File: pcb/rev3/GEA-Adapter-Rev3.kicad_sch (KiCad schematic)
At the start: 89 parts, among them J1 8P8C, J2 1x6, J3 TC2030, J4 USB_C_Receptacle_USB2.0_16P, Q1 Si2309CDS, Q2 Si2309CDS, SW1 SW_Push, SW2 SW_Push, U2 ESP32-C3-WROOM-02, U4 74LVC2G07, U5 74LVC2G07_3v3, U6 AP2112K-3.3, U7 USBLC6-2SC6, U8 AP63205WU

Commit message: feat(pcb): add rev3a automatic power and USB design
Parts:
- removed C8: 1u, Capacitor_SMD:C_0805_2012Metric, symbol Device:C
- removed D12, D13: BZX84C12LT1G, Package_TO_SOT_SMD:SOT-23, symbol Diode:BZX84Cxx
- removed D7: DNI, Diode_SMD:D_SMA, symbol Device:D_TVS
- removed JP2: AltPwr, Jumper:SolderJumper-3_P1.3mm_Bridged12_RoundedPad1.0x1.5mm_NumberLabels, symbol Jumper:SolderJumper_3_Bridged12
- removed Q1, Q2: Si2309CDS, Package_TO_SOT_SMD:SOT-23, symbol Device:Q_PMOS_GSD
- removed R30, R9: 9.1k, Resistor_SMD:R_0805_2012Metric, symbol Device:R
- removed R8: DNP, Resistor_SMD:R_0805_2012Metric, symbol Device:R
- added C18, C19: 100pF, Capacitor_SMD:C_0402_1005Metric, symbol Device:C
- added C20, C21: 1u 50V X7R, Capacitor_SMD:C_0805_2012Metric, symbol Device:C
- added C22, C23: 22nF, Capacitor_SMD:C_0402_1005Metric, symbol Device:C
- added C24, C25: 100nF, Capacitor_SMD:C_0805_2012Metric, symbol Device:C
- added D14, D15, D16, D17: MBR0540-TP, Diode_SMD:D_SOD-123, symbol Diode:MBR0540
- added Q3, Q4: CJ3407, Package_TO_SOT_SMD:SOT-23, symbol Device:Q_PMOS_GSD
- added Q5: MMBT3904, Package_TO_SOT_SMD:SOT-23, symbol Transistor_BJT:MMBT3904
- added R31, R32: 5.1k, Resistor_SMD:R_0805_2012Metric, symbol Device:R
- added R33, R34: 51R, Resistor_SMD:R_0805_2012Metric, symbol Device:R
- added R35, R36, R37: 10k, Resistor_SMD:R_0805_2012Metric, symbol Device:R
- added TP10: PIN1_PROTECTED, TestPoint:TestPoint_Pad_D1.0mm, symbol Connector:TestPoint
- added TP11: PIN3_PROTECTED, TestPoint:TestPoint_Pad_D1.0mm, symbol Connector:TestPoint
- added TP12: PIN1_SW_OUT, TestPoint:TestPoint_Pad_D1.0mm, symbol Connector:TestPoint
- added TP13: PIN3_SW_OUT, TestPoint:TestPoint_Pad_D1.0mm, symbol Connector:TestPoint
- added TP14: USB_VBUS, TestPoint:TestPoint_Pad_D1.0mm, symbol Connector:TestPoint
- added TP8: PIN1_FUSED, TestPoint:TestPoint_Pad_D1.0mm, symbol Connector:TestPoint
- added TP9: PIN3_FUSED, TestPoint:TestPoint_Pad_D1.0mm, symbol Connector:TestPoint
- added U10, U9: TPS22810DBVR, Package_TO_SOT_SMD:SOT-23-6, symbol Power_Management:TPS22810DBV
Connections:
- net p1 is gone; now on net V_INPUT: TP3.1
- net GND: now also C20.2, C21.2, C22.2, C23.2, C24.2, C25.2, D16.1 (K), D17.1 (K), Q5.2 (E), R37.2, U10.2 (GND), U9.2 (GND)
- net USB_VBUS: now also TP14.1
- net PIN1_FUSED: now reaches F2.2
- net PIN1_FUSED: now also C18.1, Q3.2 (S), R31.1, TP8.1
- net PIN3_FUSED: now reaches F1.2
- net PIN3_FUSED: now also C19.1, Q4.2 (S), R32.1, TP9.1
- net APPLIANCE_PROTECTED renamed V_INPUT
- net V_INPUT: now also D14.1 (K), D15.1 (K)
- net MCU_USB_DN renamed USB_MCU_N
- net MCU_USB_DP renamed USB_MCU_P
- net USB_DN_CONN renamed USB_CONN_N
- net USB_DN_PROTECTED renamed USB_PROTECTED_N
- net USB_DP_CONN renamed USB_CONN_P
- net USB_DP_PROTECTED renamed USB_PROTECTED_P
- new net PIN1_CT: C22.1, U9.4 (CT)
- new net PIN1_GATE: Q3.1 (G), R33.2
- new net PIN1_GATE_CLAMP: C18.2, D16.2 (A), R31.2, R33.1
- new net PIN1_PROTECTED: C20.1, Q3.3 (D), R35.1, TP10.1, U9.1 (VIN), U9.3 (EN/UVLO)
- new net PIN1_SW_OUT: C24.1, D14.2 (A), TP12.1, U9.6 (VOUT)
- new net PIN3_CT: C23.1, U10.4 (CT)
- new net PIN3_EN: Q5.3 (C), R36.2, U10.3 (EN/UVLO)
- new net PIN3_GATE: Q4.1 (G), R34.2
- new net PIN3_GATE_CLAMP: C19.2, D17.2 (A), R32.2, R34.1
- new net PIN3_PROTECTED: C21.1, Q4.3 (D), R36.1, TP11.1, U10.1 (VIN)
- new net PIN3_SW_OUT: C25.1, D15.2 (A), TP13.1, U10.6 (VOUT)
- new net PRIORITY_BASE: Q5.1 (B), R35.2, R37.1
- no-connect marks 10 -> 12
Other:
- note added: "DIAGNOSTIC TEST PADS Optional top-side SMD pads for bring-up"

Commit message: fix(pcb): align rev3a appliance connector metadata
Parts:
- J1: footprint Connector_RJ:RJ45_Amphenol_54602-x08_Horizontal -> OnionStraws:RJ45_EVERCOM_5301-8P8C_Horizontal; LCSC C2847314 -> C3097717; MPN 54602-908LF -> 5301-8P8C; Manufacturer Amphenol Communications Solutions -> EVERCOM
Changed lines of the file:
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@@
 			)
 		)
-		(property "Footprint" "Connector_RJ:RJ45_Amphenol_54602-x08_Horizontal"
+		(property "Footprint" "OnionStraws:RJ45_EVERCOM_5301-8P8C_Horizontal"
 			(at 43.815 94.615 90)
 			(effects
@@
 			)
 		)
-		(property "Datasheet" "https://cdn.amphenol-cs.com/media/wysiwyg/files/drawing/c-bmj-0102.pdf"
+		(property "Datasheet" "https://jlcpcb.com/partdetail/EVERCOM-53018P8C/C3097717"
 			(at 43.815 94.615 90)
 			(effects
@@
 			)
 		)
-		(property "Description" "Amphenol Cat 3 single modular jack, horizontal through-hole, 8P8C, unshielded"
+		(property "Description" "EVERCOM horizontal through-hole 8P8C appliance connector"
 			(at 43.815 95.25 0)
 			(effects
@@
 			)
 		)
-		(property "LCSC" "C2847314"
+		(property "LCSC" "C3097717"
 			(at 43.815 95.25 0)
 			(effects
@@
 			)
 		)
-		(property "Manufacturer" "Amphenol Communications Solutions"
+		(property "Manufacturer" "EVERCOM"
 			(at 43.815 95.25 0)
 			(effects
@@
 			)
 		)
-		(property "MPN" "54602-908LF"
+		(property "MPN" "5301-8P8C"
 			(at 43.815 95.25 0)
 			(effects

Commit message: fix(pcb): correct rev3a capacitor sourcing
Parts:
- C10: LCSC C28233 -> C286510; MPN GCM188L81H104KA57 -> 0603B104M500NT; Manufacturer Murata -> FH
- C9: LCSC C15850 -> C303950; MPN CGA5L1X7R1H106K160AC -> 1206B106K500NT; Manufacturer TDK -> FH
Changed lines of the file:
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@@
 			)
 		)
-		(property "Datasheet" "~"
+		(property "Datasheet" "https://jlcpcb.com/partdetail/288017-1206B106K500NT/C303950"
 			(at 247.65 54.61 0)
 			(effects
@@
 			)
 		)
-		(property "Description" "C15850"
+		(property "Description" "10 uF 50 V X7R 1206 MLCC"
 			(at 247.65 54.61 0)
 			(effects
@@
 			)
 		)
-		(property "LCSC" "C15850"
+		(property "LCSC" "C303950"
 			(at 247.65 54.61 0)
 			(effects
@@
 			)
 		)
-		(property "Manufacturer" "TDK"
+		(property "Manufacturer" "FH"
 			(at 247.65 54.61 0)
 			(effects
@@
 			)
 		)
-		(property "MPN" "CGA5L1X7R1H106K160AC"
+		(property "MPN" "1206B106K500NT"
 			(at 247.65 54.61 0)
 			(effects
@@
 			)
 		)
-		(property "Datasheet" "~"
+		(property "Datasheet" "https://jlcpcb.com/partdetail/0603B104M500NT/C286510"
 			(at 260.35 54.61 0)
 			(effects
@@
 			)
 		)
-		(property "Description" "C28233"
+		(property "Description" "100 nF 50 V X7R 0603 MLCC"
 			(at 260.35 54.61 0)
 			(effects
@@
 			)
 		)
-		(property "LCSC" "C28233"
+		(property "LCSC" "C286510"
 			(at 260.35 54.61 0)
 			(effects
@@
 			)
 		)
-		(property "Manufacturer" "Murata"
+		(property "Manufacturer" "FH"
 			(at 260.35 54.61 0)
 			(effects
@@
 			)
 		)
-		(property "MPN" "GCM188L81H104KA57"
+		(property "MPN" "0603B104M500NT"
 			(at 260.35 54.61 0)
 			(effects

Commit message: feat(pcb): route grounds and refine rev3a sourcing
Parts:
- J4: LCSC (none) -> C2894897; MPN USB4105-GF-A -> HC-TYPE-C-16P-01A; Manufacturer GCT -> HCTL
- L1: LCSC (none) -> C412309
- U8: LCSC (none) -> C2071056
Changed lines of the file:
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@@
 			)
 		)
-		(property "Datasheet" "https://www.usb.org/sites/default/files/documents/usb_type-c.zip"
+		(property "Datasheet" "https://datasheet.lcsc.com/datasheet/pdf/7d87e82d7c94fc2f1ad4584993e52b86.pdf?productCode=C2894897"
 			(at 93.81 335.0 0)
 			(hide yes)
@@
 			)
 		)
-		(property "Description" "USB 2.0-only 16P Type-C Receptacle connector"
+		(property "Description" "HCTL USB 2.0 Type-C receptacle, 16 contacts, top mount"
 			(at 90.0 335.0 0)
 			(hide yes)
@@
 			)
 		)
-		(property "Manufacturer" "GCT"
+		(property "Manufacturer" "HCTL"
 			(at 90.0 335.0 0)
 			(effects
@@
 			)
 		)
-		(property "MPN" "USB4105-GF-A"
+		(property "MPN" "HC-TYPE-C-16P-01A"
+			(at 90.0 335.0 0)
+			(effects
+				(font
+					(size 1.27 1.27)
+				)
+				(hide yes)
+			)
+		)
+		(property "LCSC" "C2894897"
 			(at 90.0 335.0 0)
 			(effects
@@
 			)
 		)
+		(property "LCSC" "C2071056"
+			(at 250.19 80.01 0)
+			(effects
+				(font
+					(size 1.27 1.27)
+				)
+				(hide yes)
+			)
+		)
 		(property "Input_Range" "3.8V to 32V"
 			(at 250.19 80.01 0)
@@
 			(at 284.48 77.47 0)
 			(effects
+				(font
+					(size 1.27 1.27)
+				)
+				(hide yes)
+			)
+		)
+		(property "LCSC" "C412309"
+			(at 284.48 77.47 0)
+			(effects

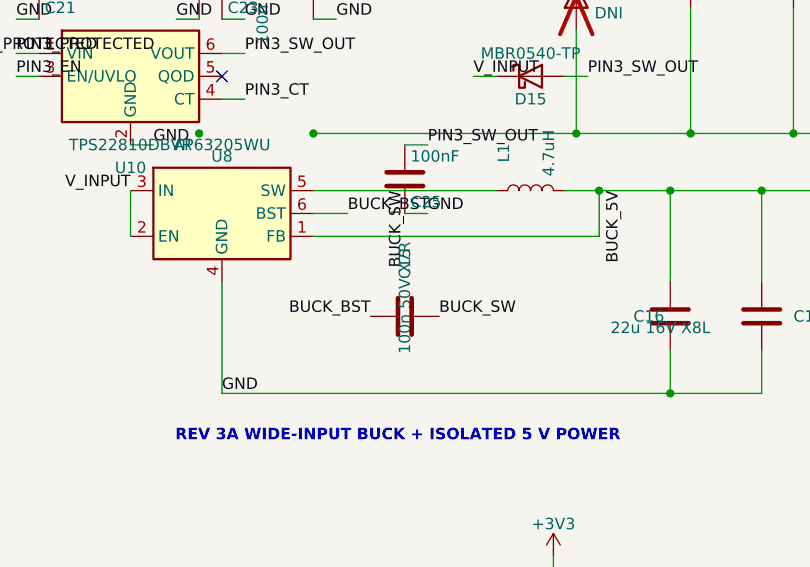
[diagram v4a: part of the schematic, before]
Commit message: fix(pcb): complete rev3a sourcing metadata
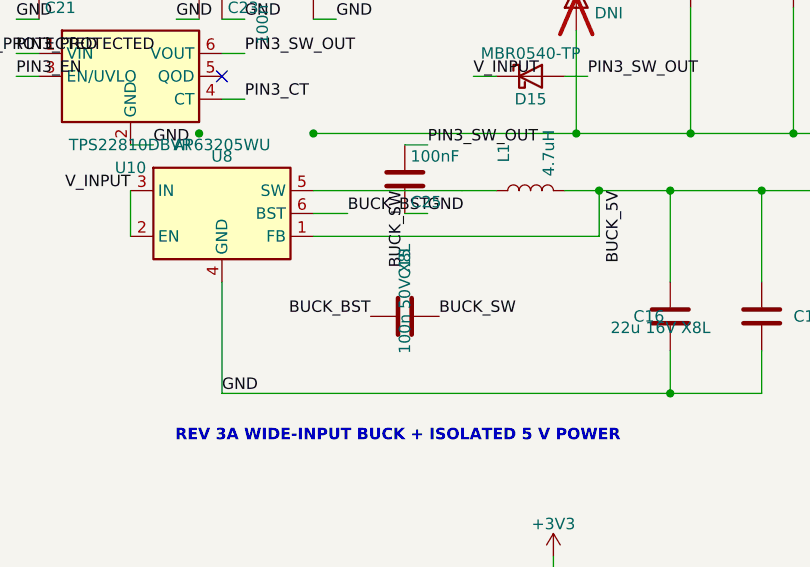
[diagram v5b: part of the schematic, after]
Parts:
- C15: value 100n 50V X7R -> 100n 50V X8L; Dielectric X7R -> X8L; LCSC (none) -> C161181
- D10, D11: LCSC (none) -> C82288
- F3: LCSC (none) -> C163512
- R26, R27: LCSC (none) -> C105580
- R28, R29: LCSC (none) -> C107701
- U7: LCSC (none) -> C7519
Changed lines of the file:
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@@
 			)
 		)
+    (property "LCSC" "C105580" (at 135.0 360.0 0)
+      (effects (font (size 1.27 1.27)) (hide yes))
+    )
 		(pin "1"
 		)
@@
 			)
 		)
+    (property "LCSC" "C105580" (at 135.0 380.0 0)
+      (effects (font (size 1.27 1.27)) (hide yes))
+    )
 		(pin "1"
 		)
@@
 			)
 		)
+    (property "LCSC" "C107701" (at 245.0 325.0 0)
+      (effects (font (size 1.27 1.27)) (hide yes))
+    )
 		(pin "1"
 		)
@@
 			)
 		)
+    (property "LCSC" "C107701" (at 245.0 345.0 0)
+      (effects (font (size 1.27 1.27)) (hide yes))
+    )
 		(pin "1"
 		)
@@
 			)
 		)
+    (property "LCSC" "C163512" (at 165.0 400.0 0)
+      (effects (font (size 1.27 1.27)) (hide yes))
+    )
 		(pin "1"
 		)
@@
 			)
 		)
+    (property "LCSC" "C7519" (at 180.0 335.0 0)
+      (effects (font (size 1.27 1.27)) (hide yes))
+    )
 		(pin "1"
 		)
@@
 			)
 		)
+    (property "LCSC" "C82288" (at 230.0 400.0 0)
+      (effects (font (size 1.27 1.27)) (hide yes))
+    )
 		(pin "1"
 		)
@@
 			)
 		)
-		(property "Value" "100n 50V X7R"
+		(property "Value" "100n 50V X8L"
 			(at 270.51 95.6 0)
 			(show_name no)
@@
 			)
 		)
-		(property "Description" "Unpolarized capacitor"
+		(property "Description" "100 nF 50 V X8L 0603 MLCC"
 			(at 270.51 91.44 0)
 			(hide yes)
@@
 			)
 		)
-		(property "Dielectric" "X7R"
+		(property "Dielectric" "X8L"
 			(at 270.51 91.44 0)
 			(effects
@@
 			)
 		)
+    (property "LCSC" "C161181" (at 270.51 91.44 0)
+      (effects (font (size 1.27 1.27)) (hide yes))
+    )
 		(pin "1"
 		)
@@
 			)
 		)
+    (property "LCSC" "C82288" (at 325.12 77.47 0)
+      (effects (font (size 1.27 1.27)) (hide yes))
+    )
 		(pin "1"
 		)

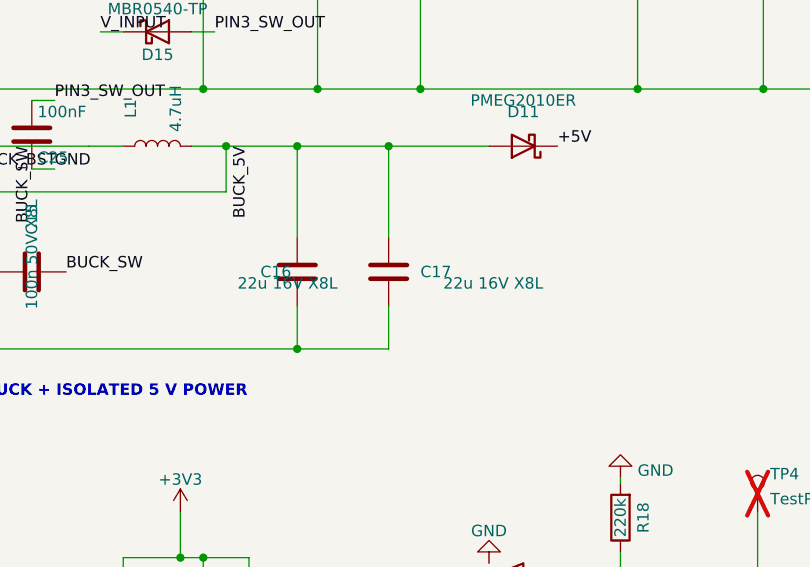
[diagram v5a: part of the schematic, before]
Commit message: fix(pcb): qualify rev3a buck capacitors
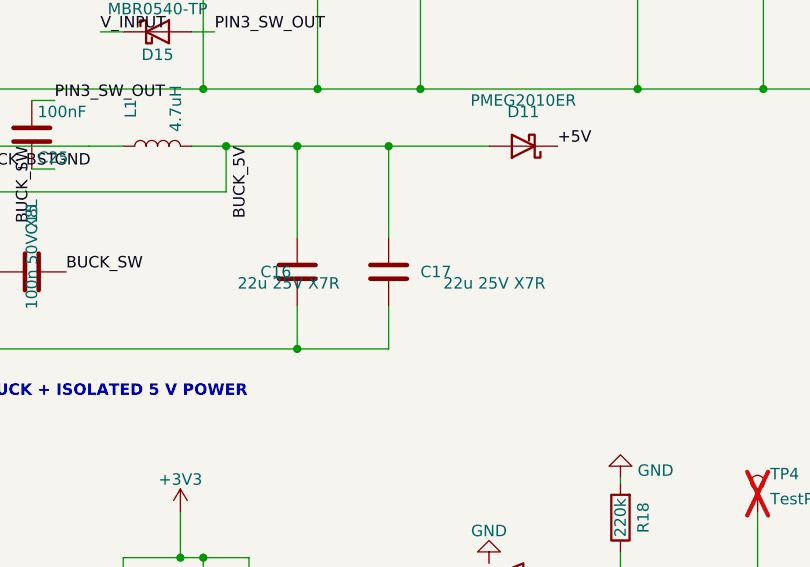
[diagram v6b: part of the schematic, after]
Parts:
- C16, C17: value 22u 16V X8L -> 22u 25V X7R; Dielectric X8L -> X7R; LCSC (none) -> C309062; MPN CGA6P1X8L1C226M250AC -> CL32B226KAJNNNE; Manufacturer TDK -> Samsung Electro-Mechanics; Tolerance (none) -> 10%; Voltage 16V -> 25V
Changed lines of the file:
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@@
 			)
 		)
-		(property "Value" "22u 16V X8L"
+		(property "Value" "22u 25V X7R"
 			(at 293.37 92.71 0)
 			(show_name no)
@@
 			)
 		)
-		(property "Datasheet" ""
-			(at 300.0 91.44 0)
-			(hide yes)
-			(show_name no)
-			(do_not_autoplace no)
-			(effects
-				(font
-					(size 1.27 1.27)
-				)
-			)
-		)
-		(property "Description" "Unpolarized capacitor"
-			(at 300.0 91.44 0)
-			(hide yes)
-			(show_name no)
-			(do_not_autoplace no)
-			(effects
-				(font
-					(size 1.27 1.27)
-				)
-			)
-		)
-		(property "Manufacturer" "TDK"
-			(at 300.0 91.44 0)
-			(effects
-				(font
-					(size 1.27 1.27)
-				)
-				(hide yes)
-			)
-		)
-		(property "MPN" "CGA6P1X8L1C226M250AC"
-			(at 300.0 91.44 0)
-			(effects
-				(font
-					(size 1.27 1.27)
-				)
-				(hide yes)
-			)
-		)
-		(property "Voltage" "16V"
-			(at 300.0 91.44 0)
-			(effects
-				(font
-					(size 1.27 1.27)
-				)
-				(hide yes)
-			)
-		)
-		(property "Dielectric" "X8L"
-			(at 300.0 91.44 0)
-			(effects
-				(font
-					(size 1.27 1.27)
-				)
-				(hide yes)
-			)
-		)
+		(property "Datasheet" "https://product.samsungsem.com/mlcc/CL32B226KAJNNN.do"
+			(at 300.0 91.44 0)
+			(hide yes)
+			(show_name no)
+			(do_not_autoplace no)
+			(effects
+				(font
+					(size 1.27 1.27)
+				)
+			)
+		)
+		(property "Description" "22 uF 25 V X7R 1210 MLCC"
+			(at 300.0 91.44 0)
+			(hide yes)
+			(show_name no)
+			(do_not_autoplace no)
+			(effects
+				(font
+					(size 1.27 1.27)
+				)
+			)
+		)
+		(property "Manufacturer" "Samsung Electro-Mechanics"
+			(at 300.0 91.44 0)
+			(effects
+				(font
+					(size 1.27 1.27)
+				)
+				(hide yes)
+			)
+		)
+		(property "MPN" "CL32B226KAJNNNE"
+			(at 300.0 91.44 0)
+			(effects
+				(font
+					(size 1.27 1.27)
+				)
+				(hide yes)
+			)
+		)
+		(property "Voltage" "25V"
+			(at 300.0 91.44 0)
+			(effects
+				(font
+					(size 1.27 1.27)
+				)
+				(hide yes)
+			)
+		)
+		(property "Dielectric" "X7R"
+			(at 300.0 91.44 0)
+			(effects
+				(font
+					(size 1.27 1.27)
+				)
+				(hide yes)
+			)
+		)
+    (property "LCSC" "C309062" (at 300.0 91.44 0)
+      (effects (font (size 1.27 1.27)) (hide yes))
+    )
+    (property "Tolerance" "10%" (at 300.0 91.44 0)
+      (effects (font (size 1.27 1.27)) (hide yes))
+    )
 		(pin "1"
 		)
@@
 			)
 		)
-		(property "Value" "22u 16V X8L"
+		(property "Value" "22u 25V X7R"
 			(at 316.23 92.71 0)
 			(show_name no)
@@
 			)
 		)
-		(property "Datasheet" ""
-			(at 310.16 91.44 0)
-			(hide yes)
-			(show_name no)
-			(do_not_autoplace no)
-			(effects
-				(font
-					(size 1.27 1.27)
-				)
-			)
-		)
-		(property "Description" "Unpolarized capacitor"
-			(at 310.16 91.44 0)
-			(hide yes)
-			(show_name no)
-			(do_not_autoplace no)
-			(effects
-				(font
-					(size 1.27 1.27)
-				)
-			)
-		)
-		(property "Manufacturer" "TDK"
-			(at 310.16 91.44 0)
-			(effects
-				(font
-					(size 1.27 1.27)
-				)
-				(hide yes)
-			)
-		)
-		(property "MPN" "CGA6P1X8L1C226M250AC"
-			(at 310.16 91.44 0)
-			(effects
-				(font
-					(size 1.27 1.27)
-				)
-				(hide yes)
-			)
-		)
-		(property "Voltage" "16V"
-			(at 310.16 91.44 0)
-			(effects
-				(font
-					(size 1.27 1.27)
-				)
-				(hide yes)
-			)
-		)
-		(property "Dielectric" "X8L"
-			(at 310.16 91.44 0)
-			(effects
-				(font
-					(size 1.27 1.27)
-				)
-				(hide yes)
-			)
-		)
+		(property "Datasheet" "https://product.samsungsem.com/mlcc/CL32B226KAJNNN.do"
+			(at 310.16 91.44 0)
+			(hide yes)
+			(show_name no)
+			(do_not_autoplace no)
+			(effects
+				(font
+					(size 1.27 1.27)
+				)
+			)
+		)
+		(property "Description" "22 uF 25 V X7R 1210 MLCC"
+			(at 310.16 91.44 0)
+			(hide yes)
+			(show_name no)
+			(do_not_autoplace no)
+			(effects
+				(font
+					(size 1.27 1.27)
+				)
+			)
+		)
+		(property "Manufacturer" "Samsung Electro-Mechanics"
+			(at 310.16 91.44 0)
+			(effects
+				(font
+					(size 1.27 1.27)
+				)
+				(hide yes)
+			)
+		)
+		(property "MPN" "CL32B226KAJNNNE"
+			(at 310.16 91.44 0)
+			(effects
+				(font
+					(size 1.27 1.27)
+				)
+				(hide yes)
+			)
+		)
+		(property "Voltage" "25V"
+			(at 310.16 91.44 0)
+			(effects
+				(font
+					(size 1.27 1.27)
+				)
+				(hide yes)
+			)
+		)
+		(property "Dielectric" "X7R"
+			(at 310.16 91.44 0)
+			(effects
+				(font
+					(size 1.27 1.27)
+				)
+				(hide yes)
+			)
+		)
+    (property "LCSC" "C309062" (at 310.16 91.44 0)
+      (effects (font (size 1.27 1.27)) (hide yes))
+    )
+    (property "Tolerance" "10%" (at 310.16 91.44 0)
+      (effects (font (size 1.27 1.27)) (hide yes))
+    )
 		(pin "1"
 		)

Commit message: fix(pcb): reconcile rev3a schematic parity
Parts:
- J4: footprint Connector_USB:USB_C_Receptacle_GCT_USB4105-xx-A_16P_TopMnt_Horizontal -> Connector_USB:USB_C_Receptacle_HCTL_HC-TYPE-C-16P-01A
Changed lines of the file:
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@@
 			)
 		)
-		(property "Footprint" "Connector_USB:USB_C_Receptacle_GCT_USB4105-xx-A_16P_TopMnt_Horizontal"
+		(property "Footprint" "Connector_USB:USB_C_Receptacle_HCTL_HC-TYPE-C-16P-01A"
 			(at 93.81 335.0 0)
 			(hide yes)

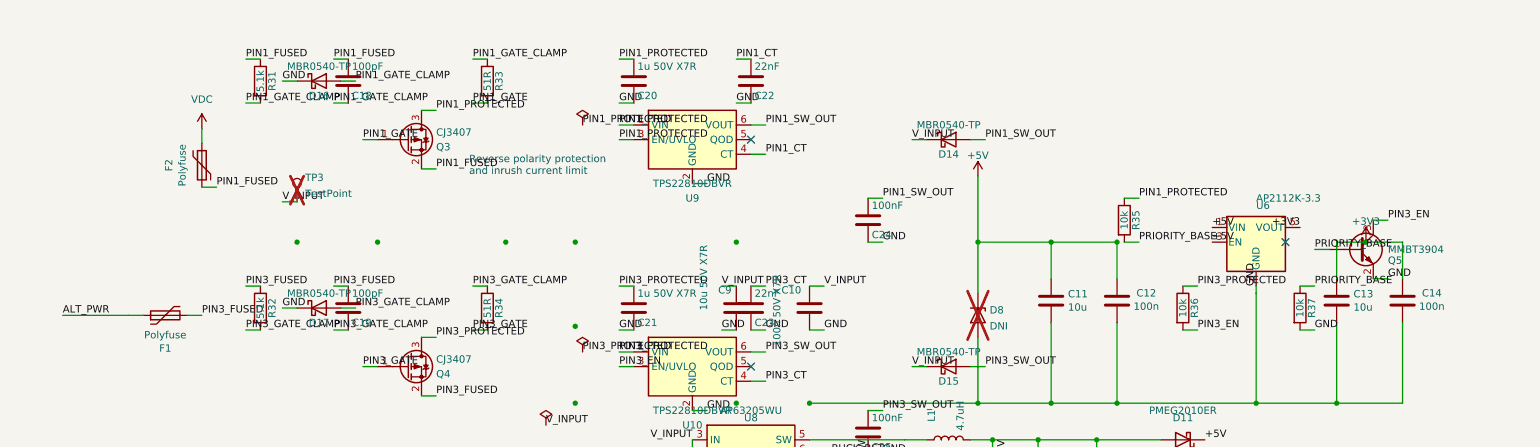
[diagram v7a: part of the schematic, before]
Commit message: docs(pcb): finalize rev3a bom metadata
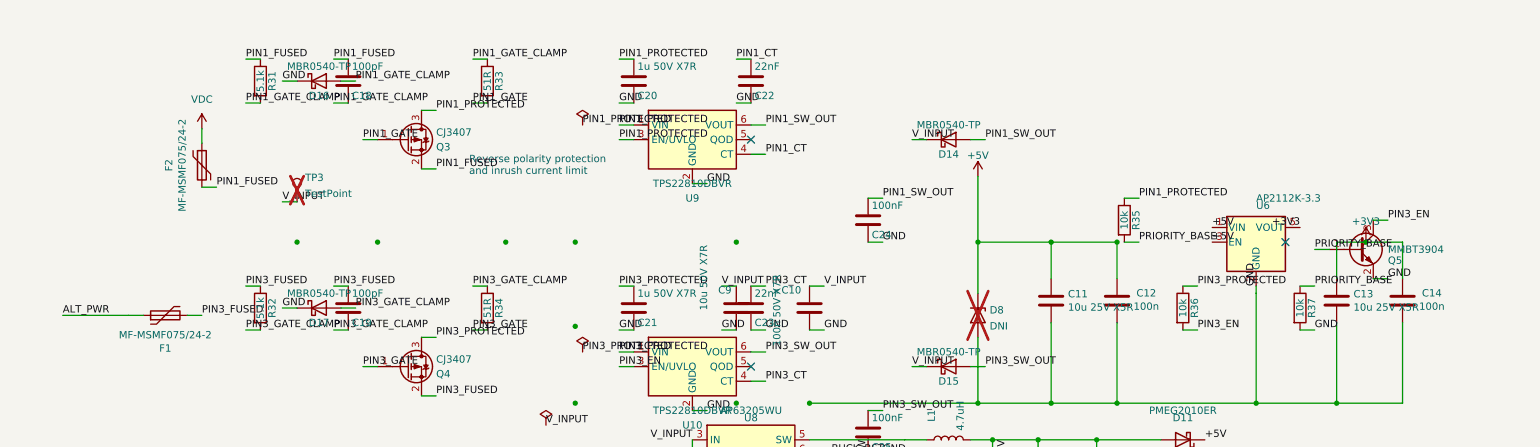
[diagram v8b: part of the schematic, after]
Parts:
- C1, C12, C14, C3, C4, C5, C6, C7: MPN (none) -> CL21B104KCFNNNE; Manufacturer (none) -> Samsung Electro-Mechanics
- C11, C13: value 10u -> 10u 25V X5R; MPN (none) -> CL21A106KAYNNNE; Manufacturer (none) -> Samsung
- C2, C20, C21: MPN (none) -> CL21B105KBFNNNE; Manufacturer (none) -> Samsung
- F1, F2: value Polyfuse -> MF-MSMF075/24-2; LCSC C12604 -> C208467; MPN (none) -> MF-MSMF075/24-2; Manufacturer (none) -> Bourns
- R1, R14, R15, R16, R17, R19, R2, R20, R3, R5: MPN (none) -> 0805W8F1002T5E; Manufacturer (none) -> UNI-ROYAL
- R10, R11, R12, R13, R23, R24, R25: MPN (none) -> 0805W8F1001T5E; Manufacturer (none) -> UNI-ROYAL
- R18, R21: LCSC C17539 -> C104108; MPN (none) -> RTT052203FTP; Manufacturer (none) -> RALEC
- R22: LCSC C17713 -> C17673; MPN (none) -> 0805W8F4701T5E; Manufacturer (none) -> UNI-ROYAL
- R4, R6, R7: MPN (none) -> 0805W8F2200T5E; Manufacturer (none) -> UNI-ROYAL
- SW1, SW2: MPN (none) -> TS-1187A-B-A-B; Manufacturer (none) -> XKB Connection
